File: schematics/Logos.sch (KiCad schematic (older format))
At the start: 10 parts

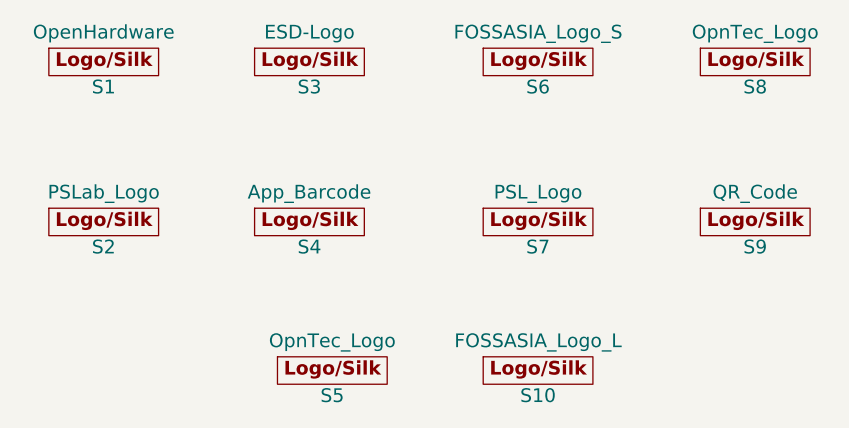
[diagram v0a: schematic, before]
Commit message: Feat: RTC Module to capture real time (#95)
* feat: RTC Module

* route: clean ups and optimization

* route: added logos

* docs: updated output files
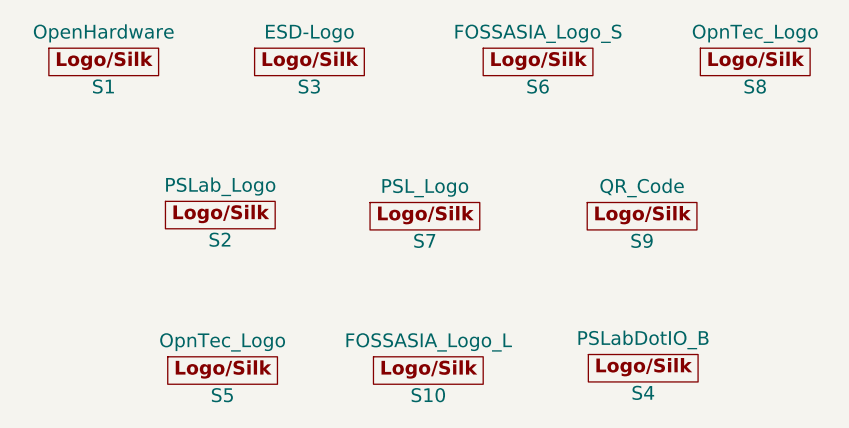
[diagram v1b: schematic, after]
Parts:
- S1: footprint Symbols:OSHW-Logo2_7.3x6mm_SilkScreen -> Symbols:OSHW-Logo_5.7x6mm_SilkScreen
- S2: footprint Custom_Components:PSLab_Logo -> Custom_Components:PSLabDotIO
- S4: value App_Barcode -> PSLabDotIO_B; footprint Custom_Components:Barcode -> Custom_Components:PSLabDotIO4000
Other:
- moved on the sheet: S10, S2, S5, S7, S9
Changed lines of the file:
@@
 F 0 "S1" H 4560 2725 60  0000 C CNN
 F 1 "OpenHardware" H 4560 2965 60  0000 C CNN
-F 2 "Symbols:OSHW-Logo2_7.3x6mm_SilkScreen" H 4560 2845 60  0001 C CNN
+F 2 "Symbols:OSHW-Logo_5.7x6mm_SilkScreen" H 4560 2845 60  0001 C CNN
 F 3 "" H 4560 2845 60  0001 C CNN
 	1    4560 2845
@@
 L PSLab:Logos S2
 U 1 1 5C27C95E
-P 4560 3545
-F 0 "S2" H 4560 3425 60  0000 C CNN
-F 1 "PSLab_Logo" H 4560 3665 60  0000 C CNN
-F 2 "Custom_Components:PSLab_Logo" H 4560 3545 60  0001 C CNN
-F 3 "" H 4560 3545 60  0001 C CNN
-	1    4560 3545
-	1    0    0    -1
-$EndComp
-$Comp
-L PSLab:Logos S4
-U 1 1 5C27C964
-P 5460 3545
-F 0 "S4" H 5460 3425 60  0000 C CNN
-F 1 "App_Barcode" H 5460 3665 60  0000 C CNN
-F 2 "Custom_Components:Barcode" H 5460 3545 60  0001 C CNN
-F 3 "" H 5460 3545 60  0001 C CNN
-	1    5460 3545
+P 5070 3515
+F 0 "S2" H 5070 3395 60  0000 C CNN
+F 1 "PSLab_Logo" H 5070 3635 60  0000 C CNN
+F 2 "Custom_Components:PSLabDotIO" H 5070 3515 60  0001 C CNN
+F 3 "" H 5070 3515 60  0001 C CNN
+	1    5070 3515
 	1    0    0    -1
 $EndComp
@@
 L PSLab:Logos S7
 U 1 1 5C27C96A
-P 6460 3545
-F 0 "S7" H 6460 3425 60  0000 C CNN
-F 1 "PSL_Logo" H 6460 3665 60  0000 C CNN
-F 2 "Custom_Components:PSL_Logo" H 6460 3545 60  0001 C CNN
-F 3 "" H 6460 3545 60  0001 C CNN
-	1    6460 3545
+P 5965 3520
+F 0 "S7" H 5965 3400 60  0000 C CNN
+F 1 "PSL_Logo" H 5965 3640 60  0000 C CNN
+F 2 "Custom_Components:PSL_Logo" H 5965 3520 60  0001 C CNN
+F 3 "" H 5965 3520 60  0001 C CNN
+	1    5965 3520
 	1    0    0    -1
 $EndComp
@@
 L PSLab:Logos S9
 U 1 1 5C27C970
-P 7410 3545
-F 0 "S9" H 7410 3425 60  0000 C CNN
-F 1 "QR_Code" H 7410 3665 60  0000 C CNN
-F 2 "Custom_Components:Website_QR" H 7410 3545 60  0001 C CNN
-F 3 "" H 7410 3545 60  0001 C CNN
-	1    7410 3545
+P 6915 3520
+F 0 "S9" H 6915 3400 60  0000 C CNN
+F 1 "QR_Code" H 6915 3640 60  0000 C CNN
+F 2 "Custom_Components:Website_QR" H 6915 3520 60  0001 C CNN
+F 3 "" H 6915 3520 60  0001 C CNN
+	1    6915 3520
 	1    0    0    -1
 $EndComp
@@
 L PSLab:Logos S5
 U 1 1 5C27C986
-P 5560 4195
-F 0 "S5" H 5560 4075 60  0000 C CNN
-F 1 "OpnTec_Logo" H 5560 4315 60  0000 C CNN
-F 2 "Custom_Components:OpnTec_Logo" H 5560 4195 60  0001 C CNN
-F 3 "" H 5560 4195 60  0001 C CNN
-	1    5560 4195
+P 5080 4195
+F 0 "S5" H 5080 4075 60  0000 C CNN
+F 1 "OpnTec_Logo" H 5080 4315 60  0000 C CNN
+F 2 "Custom_Components:OpnTec_Logo" H 5080 4195 60  0001 C CNN
+F 3 "" H 5080 4195 60  0001 C CNN
+	1    5080 4195
 	1    0    0    -1
 $EndComp
@@
 L PSLab:Logos S10
 U 1 1 5C27CF8C
-P 6460 4195
-F 0 "S10" H 6460 4075 60  0000 C CNN
-F 1 "FOSSASIA_Logo_L" H 6460 4315 60  0000 C CNN
-F 2 "Custom_Components:FOSSASIA_LogoL" H 6460 4195 60  0001 C CNN
-F 3 "" H 6460 4195 60  0001 C CNN
-	1    6460 4195
+P 5980 4195
+F 0 "S10" H 5980 4075 60  0000 C CNN
+F 1 "FOSSASIA_Logo_L" H 5980 4315 60  0000 C CNN
+F 2 "Custom_Components:FOSSASIA_LogoL" H 5980 4195 60  0001 C CNN
+F 3 "" H 5980 4195 60  0001 C CNN
+	1    5980 4195
 	1    0    0    -1
 $EndComp
+$Comp
+L PSLab:Logos S4
+U 1 1 5CB69B79
+P 6920 4185
+F 0 "S4" H 6920 4065 60  0000 C CNN
+F 1 "PSLabDotIO_B" H 6920 4305 60  0000 C CNN
+F 2 "Custom_Components:PSLabDotIO4000" H 6920 4185 60  0001 C CNN
+F 3 "" H 6920 4185 60  0001 C CNN
+	1    6920 4185
+	1    0    0    -1
+$EndComp
